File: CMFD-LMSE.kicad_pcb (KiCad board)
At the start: 4 copper layers, 100 x 80 mm, 132 parts, among them J1 Conn_01x02, J10 Conn_01x02, J11 Conn_01x02, J12 Conn_01x02, J2 Conn_01x02, J3 ZX62-B-5PA_33_, J4 Conn_01x02, J5 Conn_01x05, J6 Conn_01x02, J7 Conn_01x02, J8 Conn_01x02, J9 Conn_01x02, SW3 SW_SPDT, SW4 SW_Push, U1 MPM3610GQV-Z, U2 CH340E, U4 TPS2117DRLR, U5 BD33IC0WEFJ-E2, U6 MCP2562FD-H/SN, U7 STM32H503CBTx, X1 MU00525-32.768K

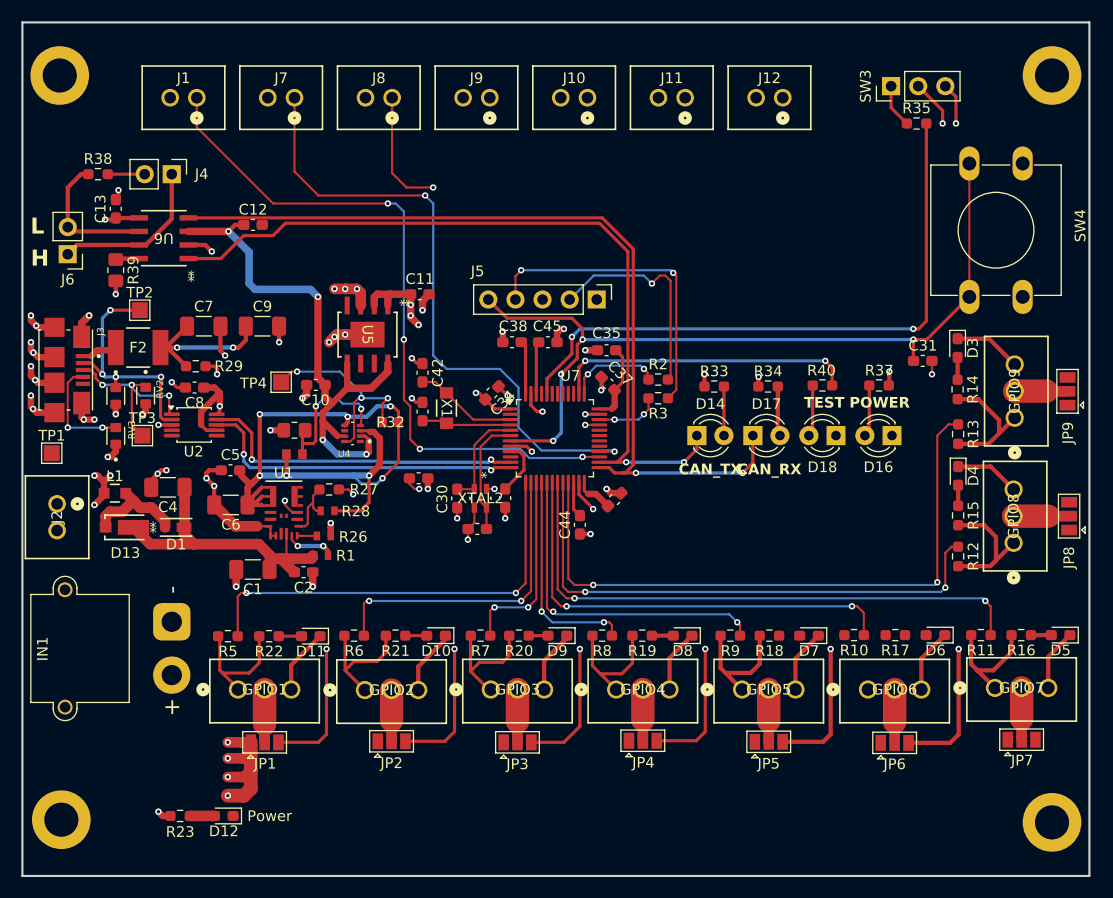
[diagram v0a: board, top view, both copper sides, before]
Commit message: DRCのエラー・警告を一部無視したけど問題ないよね
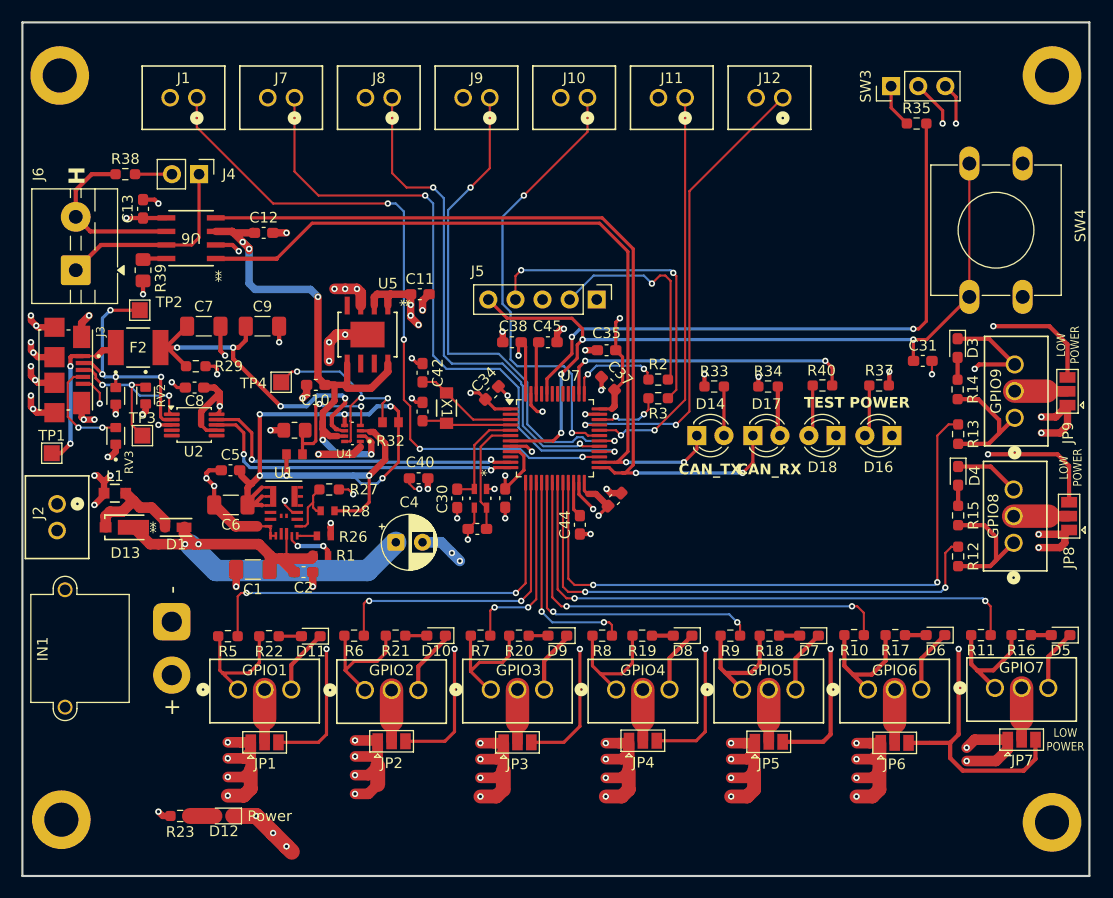
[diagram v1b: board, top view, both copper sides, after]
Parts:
- C4: footprint Capacitor_SMD:C_1206_3216Metric_Pad1.33x1.80mm_HandSolder -> Capacitor_THT:CP_Radial_D5.0mm_P2.50mm
- J6: footprint Connector_PinHeader_2.54mm:PinHeader_1x02_P2.54mm_Vertical -> TerminalBlock:TerminalBlock_MaiXu_MX126-5.0-02P_1x02_P5.00mm
- moved C4 22.0 mm to (128.0, 110.2), turned to 0 degrees
- moved C13 2.56 mm to (104.3, 79.0)
- moved J4 2.56 mm to (109.6, 75.8)
- moved R39 2.56 mm to (104.3, 84.8)
- moved U6 2.56 mm to (108.8, 81.8)
- moved R38 2.56 mm to (102.6, 75.8)
- moved J6 1.68 mm to (98.0, 84.8), turned to 90 degrees
- moved C12 1.25 mm to (115.6, 81.2)
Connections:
- H1 pad 1: GND -> unconnected-(H1-Pad1)
- H2 pad 1: GND -> unconnected-(H2-Pad1)
- H3 pad 1: GND -> unconnected-(H3-Pad1)
- H4 pad 1: GND -> unconnected-(H4-Pad1)
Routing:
- net +BATT: track 15.9 -> 111.2 mm, vias 5 -> 31
- net /MCU/GPIO_LM_4: track 0.00 -> 48.7 mm, vias 0 -> 2
- net /MCU/GPIO_LM_7: track 1.32 -> 44.7 mm, vias 1 -> 2
- net /MCU/GPIO_LM_5: track 0.00 -> 42.6 mm, vias 0 -> 2
- net +3.3V: track 130.4 -> 172.7 mm, vias 17 -> 23
- net /MCU/GPIO_LM_6: track 0.00 -> 37.9 mm, vias 0 -> 2
- net /MCU/GPIO_LM_3: track 11.5 -> 48.2 mm, vias 1 -> 2
- net GND: track 156.8 -> 180.7 mm, vias 60 -> 67
- net /PowerAndUSB/USB_5V: track 16.1 -> 34.5 mm, vias 2 -> 4
- net VIN: track 29.7 -> 47.4 mm, vias 0 -> 2
- net Net-(GPIO6-Pin_1): track 0.00 -> 12.0 mm
- net Net-(F2-Pad1): track 3.63 -> 15.1 mm, vias 0 -> 2
- net Net-(J4-Pin_1): track 15.3 -> 19.4 mm
- net /CAN/CAN_RX: track 82.0 -> 79.4 mm
- net /CAN/CAN_TX: track 75.3 -> 72.8 mm
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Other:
- board text added: "LOW POWER"
- board text removed: "L"

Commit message: 一部修正、製造ファイル出力
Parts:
- NRST: renamed from SW4; footprint Button_Switch_THT:SW_PUSH-12mm -> TactSW:TactSW_6266
- SW3: footprint Connector_PinHeader_2.54mm:PinHeader_1x03_P2.54mm_Vertical -> SlideSW:SlideSW
- moved NRST 5.57 mm to (188.6, 80.0), turned to 90 degrees
- moved SW3 3.12 mm to (177.0, 65.8), turned to 0 degrees
- moved C1 1.20 mm to (114.6, 114.0)
- moved C2 1.20 mm to (119.3, 114.2)
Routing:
- net GND: track 180.7 -> 169.5 mm, vias 67 -> 85
- net /MCU/NRST: track 78.0 -> 80.9 mm
- net +3.3V: track 172.7 -> 175.4 mm
- net VIN: track 47.4 -> 49.6 mm
- net /MCU/GPIO_1: track 40.7 -> 38.7 mm
- net Net-(SW3-B): track 4.11 -> 5.77 mm
- net /CAN/CAN_RX: track 79.4 -> 80.3 mm
- added copper zone on F.Cu, net GND
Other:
- board text added: "GND"
- board text added: "GND→"
- board text added: "GPIO"
- board text added: "ON"
- board text added: "PA15"
- board text added: "PW"
- board text added: "SIG"
- board text added: "←3.3V"
- board text added: "リミット"
- board text removed: "POWER"
- board text removed: "TEST"

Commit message: すまんかった
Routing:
- net +BATT: track 111.2 -> 108.7 mm
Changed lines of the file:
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@@
-	)
-	(segment
-		(start 185.35 128.75)
-		(end 185.35 129.65)
-		(width 1)
-		(layer "F.Cu")
-		(net "+BATT")
 	)
 	(segment
@@
 		(width 1)
 		(layer "F.Cu")
-		(net "+BATT")
-	)
-	(segment
-		(start 185.35 129.65)
-		(end 184.25 130.75)
-		(width 1)
-		(layer "F.Cu")

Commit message: ロゴを追加
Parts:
- added G***: LOGO, LOGO, B.Cu at (128.2, 106.2)
- added G***: LOGO, LOGO, B.Cu at (121.5, 85.5)
